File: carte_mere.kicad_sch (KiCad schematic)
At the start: 52 parts, among them J10 Conn_01x02_Pin, J11 Conn_01x02_Pin, J12 Conn_01x02_Pin, J13 Conn_01x02_Pin, J14 Conn_01x02, J20 Conn_01x04, J23 Conn_01x02, J24 Conn_01x02

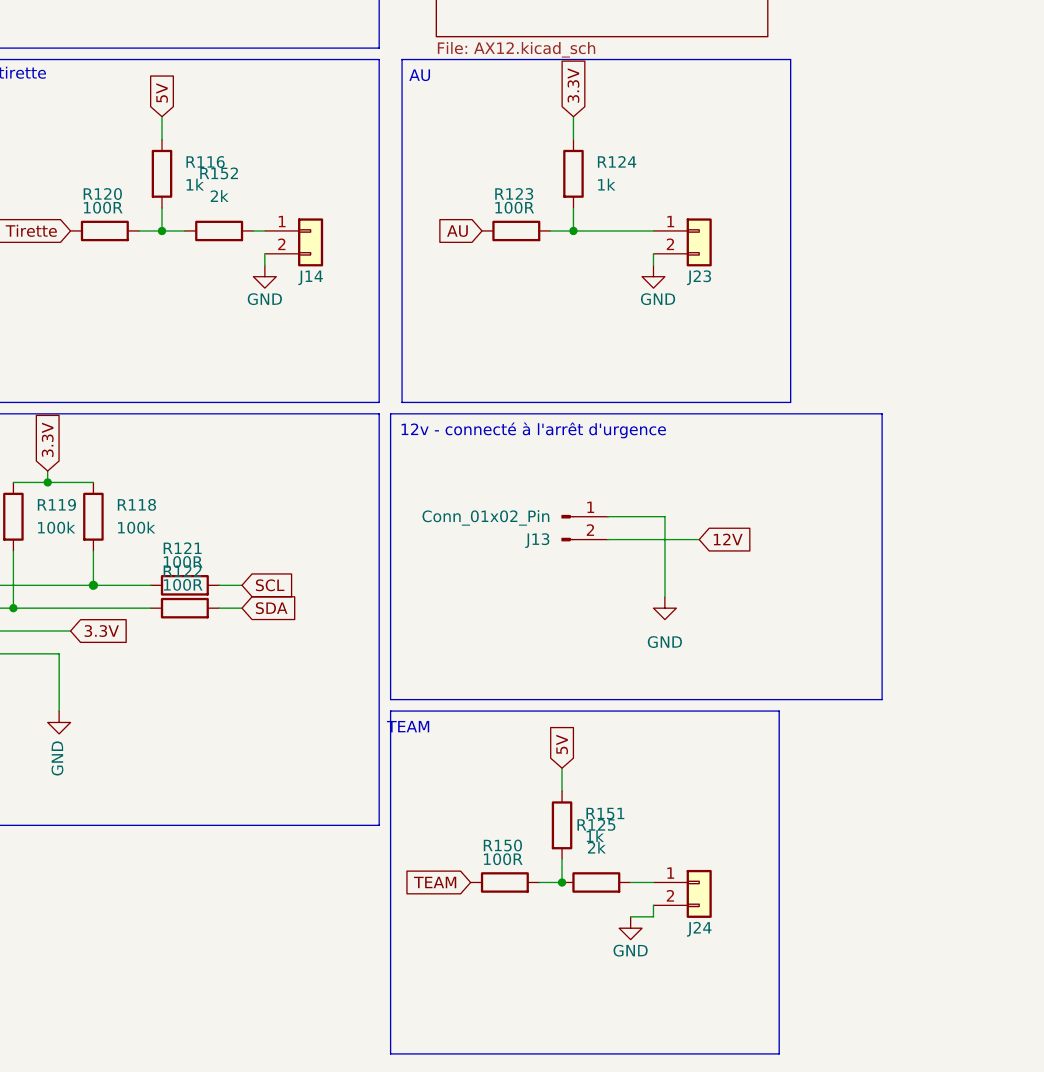
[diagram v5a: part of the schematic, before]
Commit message: fix switch issue
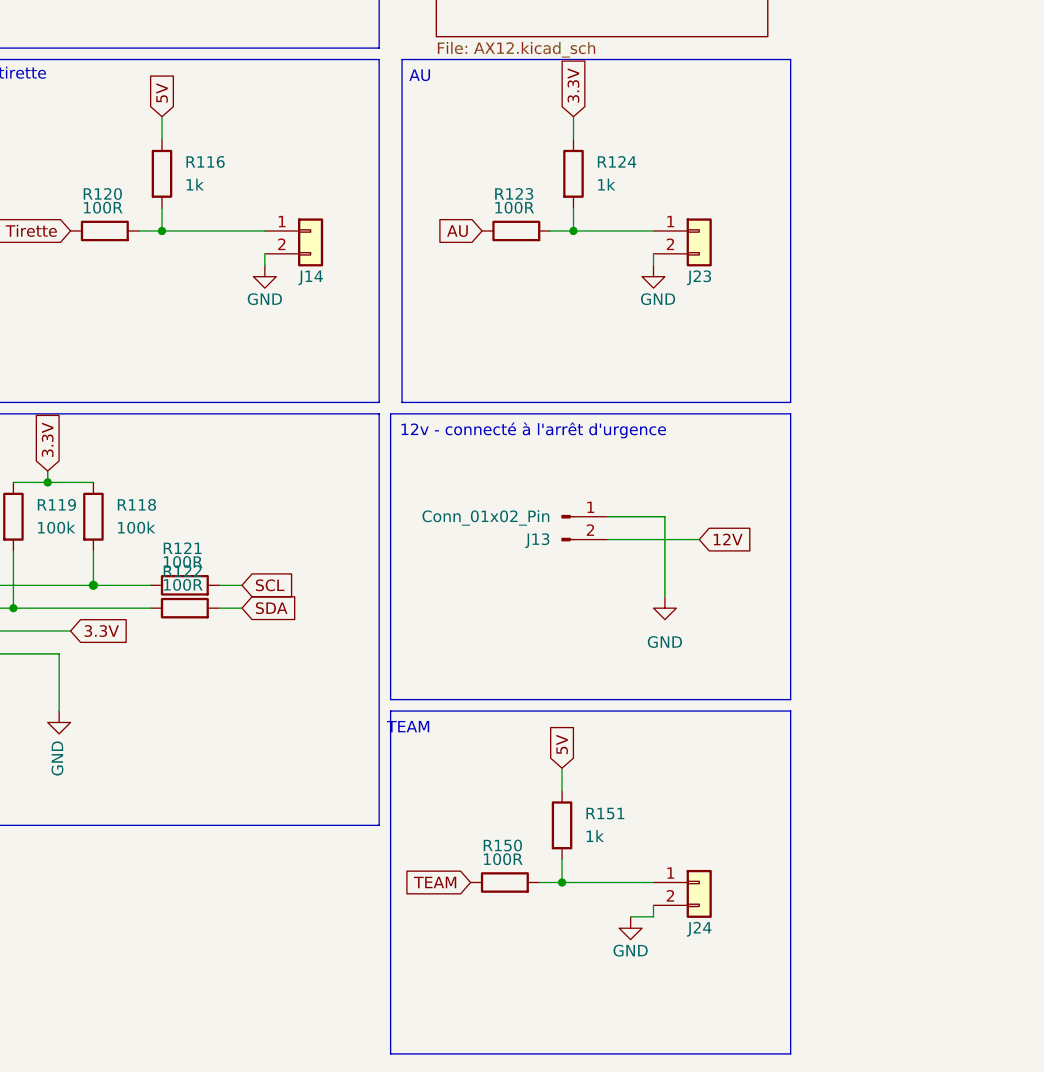
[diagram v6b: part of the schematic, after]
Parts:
- removed R125, R152: 2k, Capacitor_SMD:C_0402_1005Metric, symbol Device:R
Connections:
- net at J14.1 (Pin_1): now also R116.2, R120.2
- net at R150.2, R151.2: now also J24.1 (Pin_1)
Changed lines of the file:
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@@
 	(paper "A3")
 	(junction
-		(at 152.4 207.01)
+		(at 153.67 134.62)
 		(diameter 0)
 		(color 0 0 0 0)
 	)
 	(junction
-		(at 153.67 134.62)
+		(at 152.4 207.01)
 		(diameter 0)
 		(color 0 0 0 0)
@@
 	(wire
 		(pts
+			(xy 152.4 207.01) (xy 162.56 207.01)
+		)
+		(stroke
+			(width 0)
+			(type default)
+		)
+	)
+	(wire
+		(pts
 			(xy 257.81 39.37) (xy 256.54 39.37)
 		)
@@
 	(wire
 		(pts
-			(xy 162.56 207.01) (xy 160.02 207.01)
-		)
-		(stroke
-			(width 0)
-			(type default)
-		)
-	)
-	(wire
-		(pts
 			(xy 233.68 31.75) (xy 236.22 31.75)
 		)
@@
 	(wire
 		(pts
-			(xy 118.11 134.62) (xy 119.38 134.62)
-		)
-		(stroke
-			(width 0)
-			(type default)
-		)
-	)
-	(wire
-		(pts
 			(xy 106.68 41.91) (xy 101.6 41.91)
 		)
@@
 	(wire
 		(pts
-			(xy 107.95 134.62) (xy 110.49 134.62)
+			(xy 107.95 134.62) (xy 119.38 134.62)
 		)
 		(stroke
@@
 	(rectangle
 		(start 133.35 187.96)
-		(end 176.53 226.06)
+		(end 177.8 226.06)
 		(stroke
 			(width 0)
@@
 		(exclude_from_sim no)
 		(at 133.35 154.94 0)
-		(size 54.61 31.75)
+		(size 44.45 31.75)
 		(stroke
 			(width 0)
@@
 	(symbol
 		(lib_id "Device:R")
-		(at 114.3 134.62 90)
-		(unit 1)
-		(exclude_from_sim no)
-		(in_bom yes)
-		(on_board yes)
-		(dnp no)
-		(fields_autoplaced yes)
-		(property "Reference" "R152"
-			(at 114.3 128.27 90)
-			(effects
-				(font
-					(size 1.27 1.27)
-				)
-			)
-		)
-		(property "Value" "2k"
-			(at 114.3 130.81 90)
-			(effects
-				(font
-					(size 1.27 1.27)
-				)
-			)
-		)
-		(property "Footprint" "Capacitor_SMD:C_0402_1005Metric"
-			(at 114.3 136.398 90)
-			(effects
-				(font
-					(size 1.27 1.27)
-				)
-				(hide yes)
-			)
-		)
-		(property "Datasheet" "~"
-			(at 114.3 134.62 0)
-			(effects
-				(font
-					(size 1.27 1.27)
-				)
-				(hide yes)
-			)
-		)
-		(property "Description" "Resistor"
-			(at 114.3 134.62 0)
-			(effects
-				(font
-					(size 1.27 1.27)
-				)
-				(hide yes)
-			)
-		)
-		(pin "1"
-		)
-		(pin "2"
-		)
-		(instances
-			(project "carte_mere"
-				(path "/20c56496-71e7-4272-aa93-980e4fc2cc62"
-					(reference "R152")
-					(unit 1)
-				)
-			)
-		)
-	)
-	(symbol
-		(lib_id "Device:R")
 		(at 240.03 39.37 90)
 		(unit 1)
@@
 					(unit 1)
 				)
-			)
-		)
-	)
-	(symbol
-		(lib_id "Device:R")
-		(at 156.21 207.01 90)
-		(unit 1)
-		(exclude_from_sim no)
-		(in_bom yes)
-		(on_board yes)
-		(dnp no)
-		(fields_autoplaced yes)
-		(property "Reference" "R125"
-			(at 156.21 200.66 90)
-			(effects
-				(font
-					(size 1.27 1.27)
-				)
-			)
-		)
-		(property "Value" "2k"
-			(at 156.21 203.2 90)
-			(effects
-				(font
-					(size 1.27 1.27)
-				)
-			)
-		)
-		(property "Footprint" "Capacitor_SMD:C_0402_1005Metric"
-			(at 156.21 208.788 90)
-			(effects
-				(font
-					(size 1.27 1.27)
-				)
-				(hide yes)
-			)
-		)
-		(property "Datasheet" "~"
-			(at 156.21 207.01 0)
-			(effects
-				(font
-					(size 1.27 1.27)
-				)
-				(hide yes)
-			)
-		)
-		(property "Description" "Resistor"
-			(at 156.21 207.01 0)
-			(effects
-				(font
-					(size 1.27 1.27)
-				)
-				(hide yes)
-			)
-		)
-		(pin "1"
-		)
-		(pin "2"
-		)
-		(instances
-			(project "carte_mere"
-				(path "/20c56496-71e7-4272-aa93-980e4fc2cc62"
-					(reference "R125")
-					(unit 1)
-				)

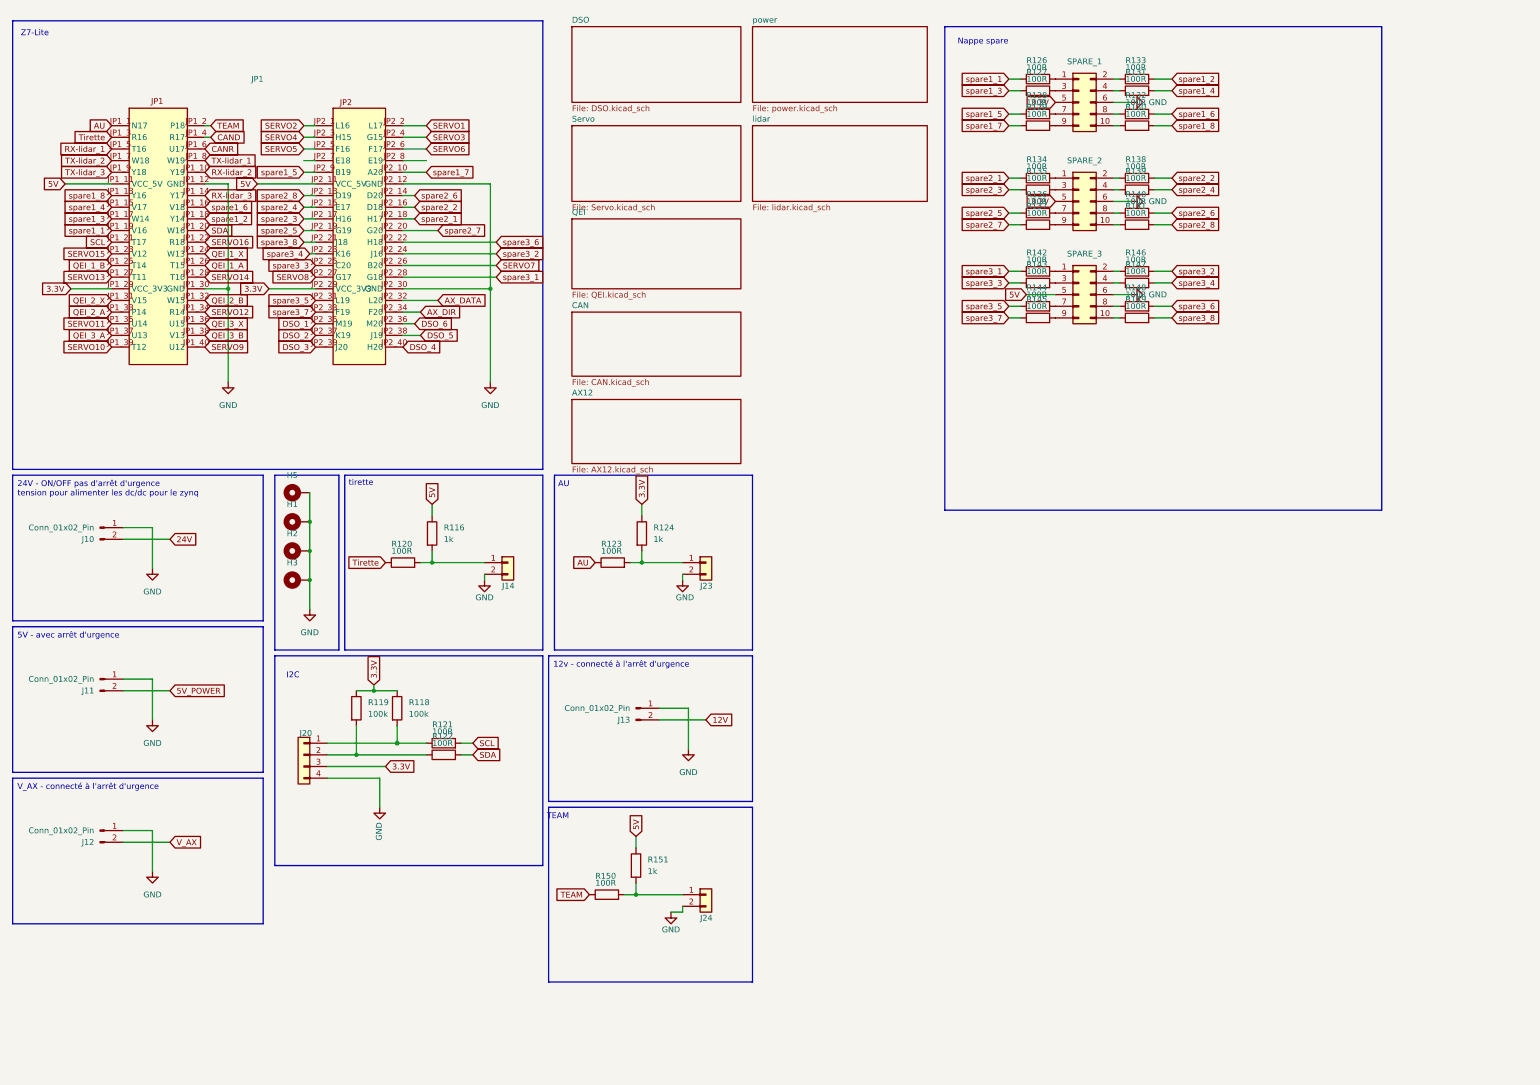
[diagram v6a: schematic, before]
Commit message: delete dso to add stepper motor controller
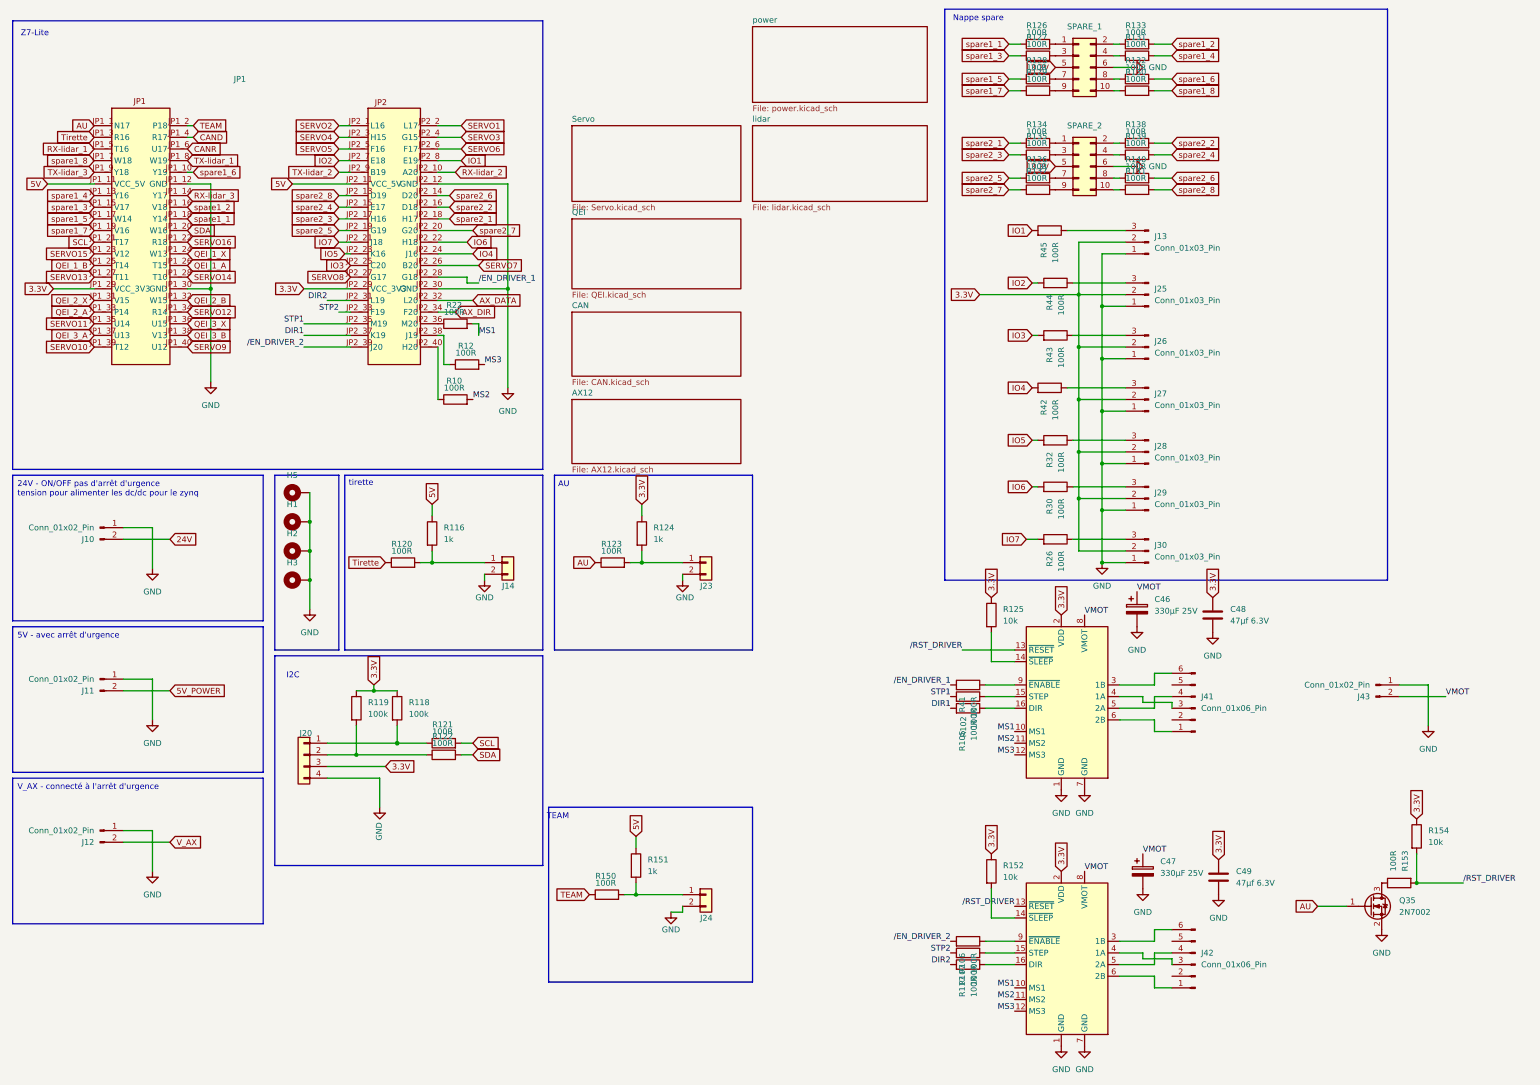
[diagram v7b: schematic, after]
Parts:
- removed J13: Conn_01x02_Pin, Connector_AMASS:AMASS_XT30U-F_1x02_P5.0mm_Vertical, symbol Connector:Conn_01x02_Pin
- removed R142, R143, R144, R145, R146, R147, R148, R149: 100R, Capacitor_SMD:C_0402_1005Metric, symbol Device:R
- removed SPARE_3: Conn_02x05_Odd_Even, Connector_PinSocket_2.54mm:PinSocket_2x05_P2.54mm_Vertical, symbol Connector_Generic:Conn_02x05_Odd_Even
- added A1, A2: Pololu_Breakout_A4988, 7Robot_lib:Pololu_Breakout-16_15.2x20.3mm, symbol Driver_Motor:Pololu_Breakout_A4988
- added C46, C47: 330µF 25V, 7Robot_lib:CP_Sided_D8.0mm_P3.50mm_L10.0mm, symbol Device:C_Polarized
- added C48, C49: 47µf 6.3V, Capacitor_SMD:C_0805_2012Metric, symbol Device:C
- added J13, J25, J26, J27, J28, J29, J30: Conn_01x03_Pin, Connector_PinHeader_2.54mm:PinHeader_1x03_P2.54mm_Vertical, symbol Connector:Conn_01x03_Pin
- added J41, J42: Conn_01x06_Pin, 7Robot_Conn:JST_PH_B6B-PH-K_1x06_P2.00mm_Vertical, symbol Connector:Conn_01x06_Pin
- added J43: Conn_01x02_Pin, Connector_AMASS:AMASS_XT30U-F_1x02_P5.0mm_Vertical, symbol Connector:Conn_01x02_Pin
- added Q35: 2N7002, Package_TO_SOT_SMD:TSOT-23, symbol Device:Q_NMOS_GSD
- added R10, R12, R22: 100R, Capacitor_SMD:C_0402_1005Metric, symbol Device:R
- added R102, R105, R106, R107, R117, R26, R30, R32, R41, R42, R43, R44, R45: 100R, Resistor_SMD:R_0402_1005Metric, symbol Device:R
- added R125, R152, R154: 10k, Resistor_SMD:R_0402_1005Metric, symbol Device:R
- added R153: 100R, Resistor_SMD:R_0603_1608Metric, symbol Device:R
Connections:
- net 3.3V: now also A1.2 (VDD), A2.2 (VDD), C48.1, C49.1, J13.2 (Pin_2), J25.2 (Pin_2), J26.2 (Pin_2), J27.2 (Pin_2), J28.2 (Pin_2), J29.2 (Pin_2), J30.2 (Pin_2), R125.1, R152.1, R154.1
- net AU: now also Q35.1 (G)
- net GND: now also A1.1 (GND), A1.7 (GND), A2.1 (GND), A2.7 (GND), C46.2, C47.2, C48.2, C49.2, J13.1 (Pin_1), J25.1 (Pin_1), J26.1 (Pin_1), J27.1 (Pin_1), J28.1 (Pin_1), J29.1 (Pin_1), J30.1 (Pin_1), J43.1 (Pin_1), Q35.2 (S)
- net RX-lidar_2: now also JP1.JP2_10 (A20); no longer JP1.JP1_10 (Y19)
- net TX-lidar_2: now also JP1.JP2_9 (B19); no longer JP1.JP1_7 (W18)
- net spare1_1: now also JP1.JP1_18 (Y14); no longer JP1.JP1_19 (V16)
- net spare1_2: now also JP1.JP1_16 (V18); no longer JP1.JP1_18 (Y14)
- net spare1_3: now also JP1.JP1_15 (V17); no longer JP1.JP1_17 (W14)
- net spare1_4: now also JP1.JP1_13 (Y16); no longer JP1.JP1_15 (V17)
- net spare1_5: now also JP1.JP1_17 (W14); no longer JP1.JP2_9 (B19)
- net spare1_6: now also JP1.JP1_10 (Y19); no longer JP1.JP1_16 (V18)
- net spare1_7: now also JP1.JP1_19 (V16); no longer JP1.JP2_10 (A20)
- net spare1_8: now also JP1.JP1_7 (W18); no longer JP1.JP1_13 (Y16)
- net IO2: now reaches JP1.JP2_7 (E18)
- net IO2: now also R44.2
- net IO1: now reaches JP1.JP2_8 (E19)
- net IO1: now also R45.2
- net DSO_1 renamed STP1
- net STP1: now also R102.2
- net DSO_2 renamed DIR1
- net DIR1: now also R105.2
- net DSO_3 renamed /EN_DRIVER_2
- net /EN_DRIVER_2: now also R106.2
- net DSO_4: no longer names the net of JP1.JP2_40 (H20)
- net DSO_4: now also R10.1
- net DSO_5: no longer names the net of JP1.JP2_38 (J19)
- net DSO_5: now also R12.1
- net DSO_6: no longer names the net of JP1.JP2_36 (M20)
- net DSO_6: now also R22.1
- net spare3_1 renamed /EN_DRIVER_1
- net /EN_DRIVER_1: now also R41.2
- net spare3_2 renamed IO4
- net IO4: now also R42.2
- net spare3_3 renamed IO3
- net IO3: now also R43.2
- net spare3_4 renamed IO5
- net IO5: now also R32.2
- net spare3_5 renamed DIR2
- net DIR2: now also R117.2
- net spare3_6 renamed IO6
- net IO6: now also R30.2
- net spare3_7 renamed STP2
- net STP2: now also R107.2
- net spare3_8 renamed IO7
- net IO7: now also R26.2
- new net: J30.3 (Pin_3), R26.1
- new net: A2.14 (~{SLEEP}), R152.2
- new net: A1.16 (DIR), R105.1
- new net: J13.3 (Pin_3), R45.1
- new net: J25.3 (Pin_3), R44.1
- new net: Q35.3 (D), R153.1
- new net: A2.16 (DIR), R117.1
- new net: A1.14 (~{SLEEP}), R125.2
- new net: A1.15 (STEP), R102.1
- new net: A1.3 (1B), J41.6 (Pin_6)
- new net: A1.4 (1A), J41.3 (Pin_3)
- new net: A1.5 (2A), J41.4 (Pin_4)
- new net: A1.6 (2B), J41.1 (Pin_1)
- new net: A1.9 (~{ENABLE}), R41.1
- new net: A2.9 (~{ENABLE}), R106.1
- new net: J27.3 (Pin_3), R42.1
- new net: J29.3 (Pin_3), R30.1
- new net: A2.6 (2B), J42.1 (Pin_1)
- new net: A2.4 (1A), J42.3 (Pin_3)
- new net: A2.5 (2A), J42.4 (Pin_4)
- new net: A2.3 (1B), J42.6 (Pin_6)
- new net: J28.3 (Pin_3), R32.1
- new net: J26.3 (Pin_3), R43.1
- new net: A2.15 (STEP), R107.1
- new net MS1: A1.10 (MS1), A2.10 (MS1), R22.2
- new net MS2: A1.11 (MS2), A2.11 (MS2), R10.2
- new net MS3: A1.12 (MS3), A2.12 (MS3), R12.2
- new net VMOT: A1.8 (VMOT), A2.8 (VMOT), C46.1, C47.1, J43.2 (Pin_2)
- new net /RST_DRIVER: A1.13 (~{RESET}), A2.13 (~{RESET}), R153.2, R154.2
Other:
- removed sheet DSO
- moved on the sheet: JP1, R126, R127, R128, R129, R130, R131, R132, R133, R134, R135, R136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
